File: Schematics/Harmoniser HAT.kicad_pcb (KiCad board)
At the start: 2 copper layers, 150 x 75 mm, 34 parts, among them J1 RPi GPIO, J10 Line In, J11 BOB21250-LEFT, J12 BOB21250-RIGHT, J6 I2C Header, J7 PWR, J8 I2S Header, J9 Line In, SW1 RotaryEncoder_Switch, SW2 RotaryEncoder_Switch, SW3 RotaryEncoder_Switch, U2 24LC256, U5 MCP23017_SP

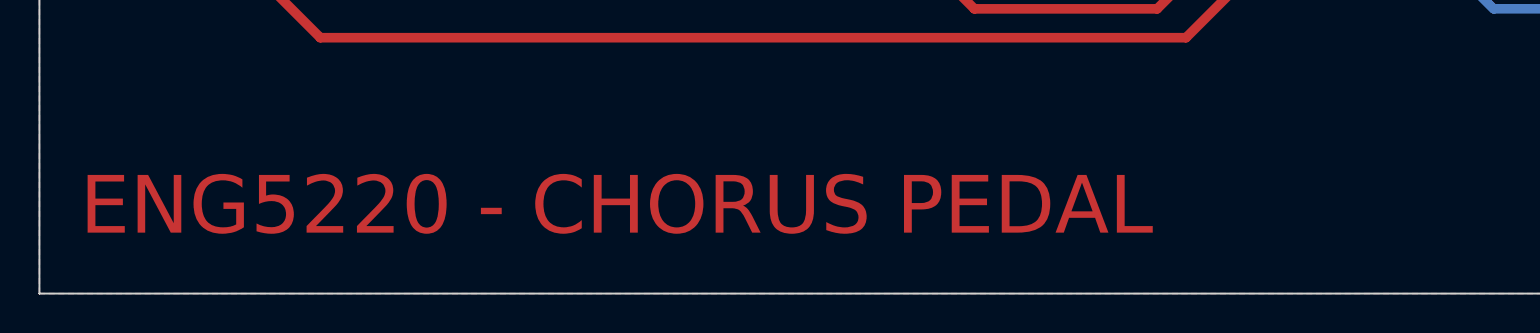
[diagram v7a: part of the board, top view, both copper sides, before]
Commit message: renamed the PCB
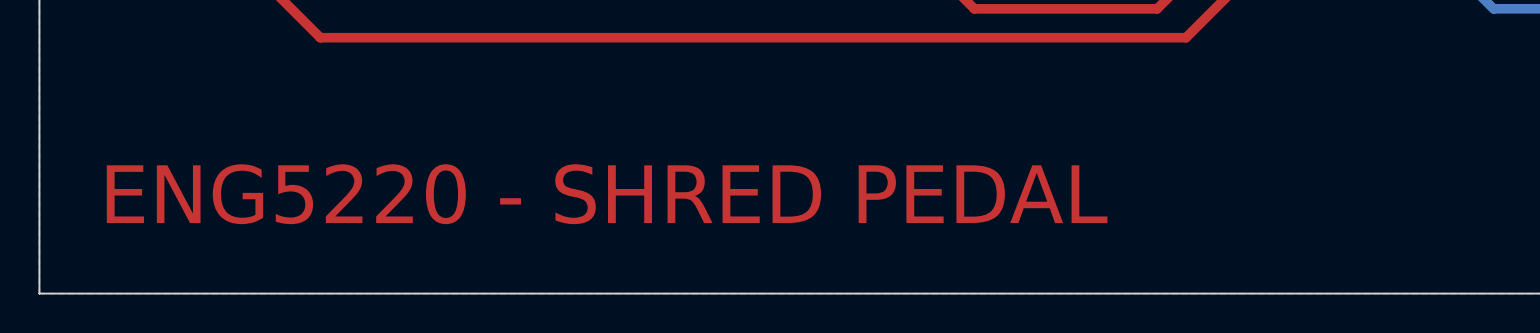
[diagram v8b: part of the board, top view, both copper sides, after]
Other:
- board text added: "ENG5220 - SHRED PEDAL"
- board text removed: "ENG5220 - CHORUS PEDAL"
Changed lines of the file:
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@@
 		(layer "Edge.Cuts")
 	)
-	(gr_text "ENG5220 - CHORUS PEDAL"
-		(at 77.5 115 0)
+	(gr_text "ENG5220 - SHRED PEDAL"
+		(at 78.5 114.5 0)
 		(layer "F.Cu")
 		(effects
@@
 		(polygon
 			(pts
-				(xy 77 109.5) (xy 142 109.5) (xy 142 116) (xy 77 116)
+				(xy 77 109.5) (xy 139.5 109.5) (xy 139.5 116) (xy 77 116)
 			)
 		)
